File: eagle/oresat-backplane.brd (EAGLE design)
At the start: 82.8 x 213.8 mm, 98 parts

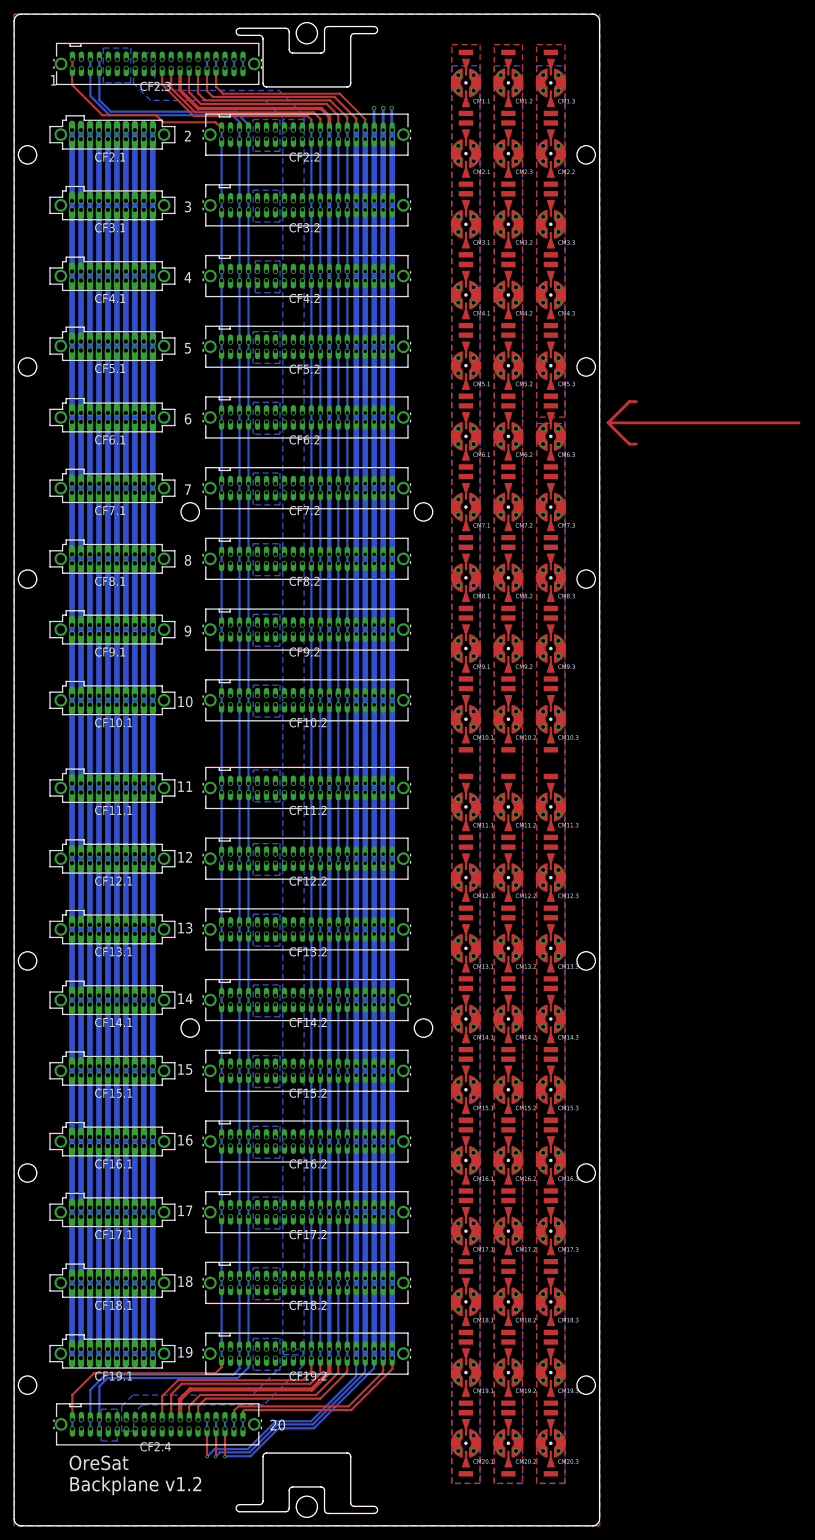
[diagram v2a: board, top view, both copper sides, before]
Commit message: Updated connector locations from MCAD. Last of the separate RF grounds before reverting back to single ground plane.
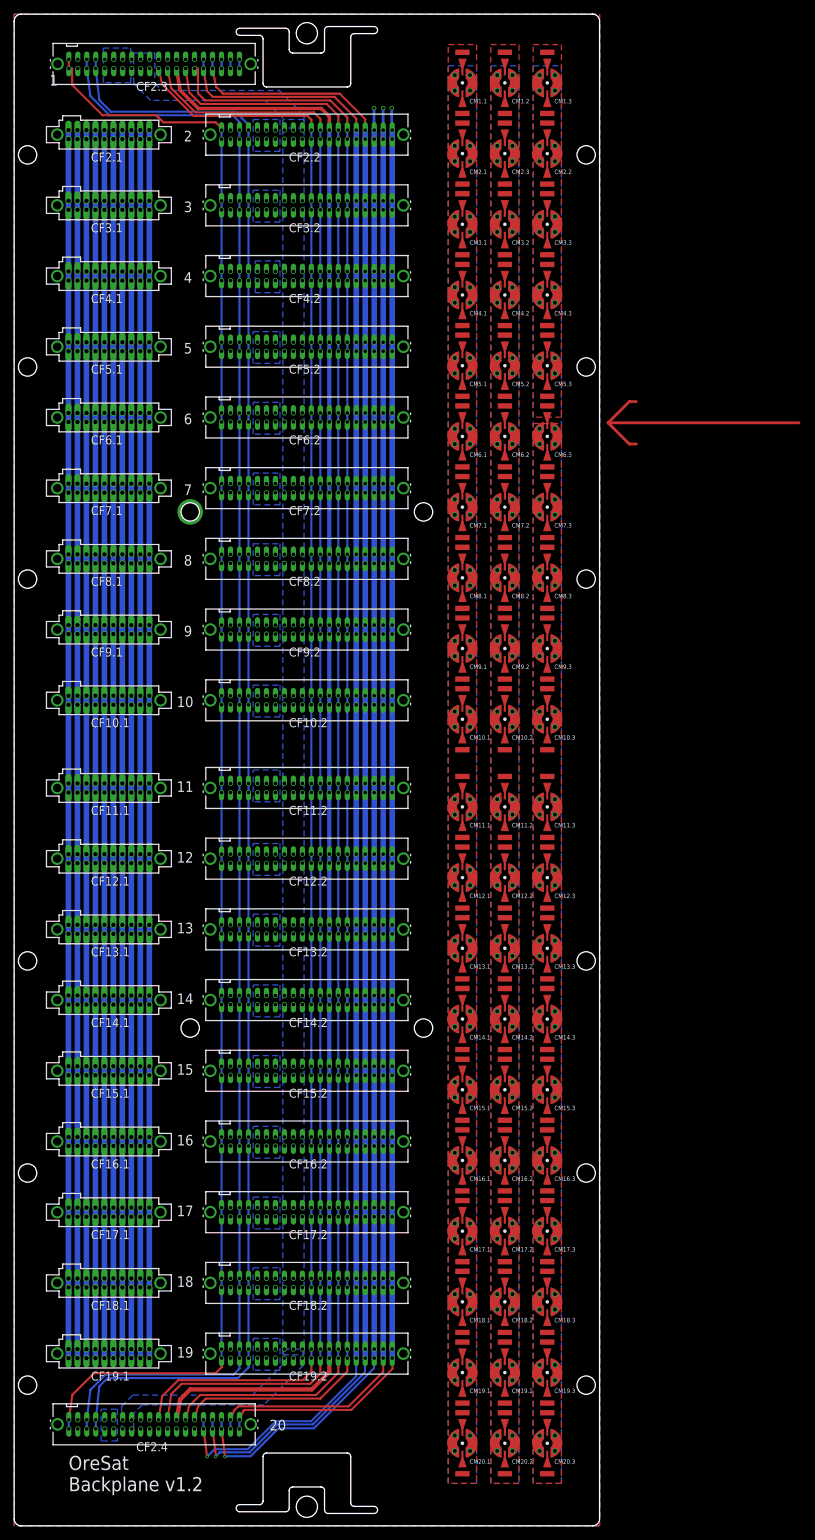
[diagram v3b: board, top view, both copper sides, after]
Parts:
- moved CF5.1 0.51 mm to (13.4, 166.8)
- moved CF10.1 0.50 mm to (13.4, 116.8)
- moved CF11.1 0.50 mm to (13.4, 104.4)
- moved CF12.1 0.50 mm to (13.4, 94.4)
- moved CF13.1 0.50 mm to (13.4, 84.4)
- moved CF14.1 0.50 mm to (13.4, 74.4)
- moved CF15.1 0.50 mm to (13.4, 64.4)
- moved CF16.1 0.50 mm to (13.4, 54.4)
- moved CF17.1 0.50 mm to (13.4, 44.4)
- moved CF18.1 0.50 mm to (13.4, 34.4)
- moved CF19.1 0.50 mm to (13.4, 24.4)
- moved CF2.1 0.50 mm to (13.4, 196.8)
- moved CF2.3 0.50 mm to (19.8, 206.8)
- moved CF2.4 0.50 mm to (19.8, 14.4)
- moved CF3.1 0.50 mm to (13.4, 186.8)
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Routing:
- net !SD: track 230.1 -> 231.0 mm
- net OPD_SDA: track 229.8 -> 230.3 mm

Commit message: Backplane v2.0! New dimensions and connector placement for Frame v1.1. New bespoke RF lines for the current OreSat RF card and antenna plan. After design review, added one more pin pair to vbus and gnd. Killed two spare pins, down to 5. Still some waffling on microsptrip width, otherwise done.
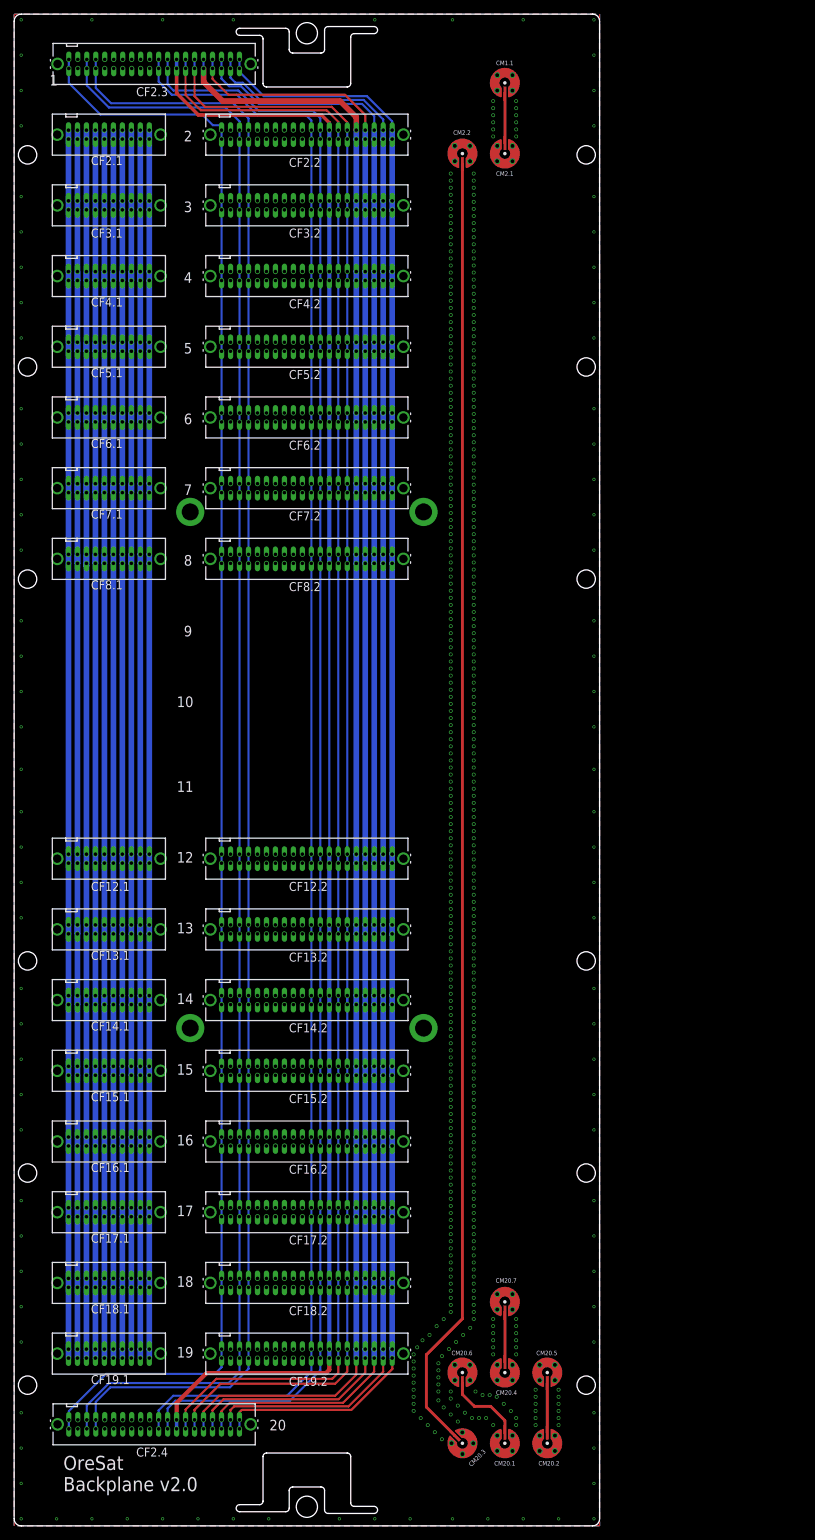
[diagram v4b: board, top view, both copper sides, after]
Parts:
- removed CF10.1, CF11.1, CF9.1: SFM-110-X1-XXX-D-LC, J-Samtec-SFM-110-X1-XXX-D-LC:SFM-110-X1-XXX-D-LC
- removed CF10.2, CF11.2, CF9.2: SFM-120-X1-XXX-D, J-Samtec-SFM-120-X1-XXX-D:SFM-120-X1-XXX-D
- removed CM1.2, CM1.3, CM10.1, CM10.2, CM10.3, CM11.1, CM11.2, CM11.3, CM12.1, CM12.2, CM12.3, CM13.1, CM13.2, CM13.3, CM14.1, CM14.2, CM14.3, CM15.1, CM15.2, CM15.3, CM16.1, CM16.2, CM16.3, CM17.1, CM17.2, CM17.3, CM18.1, CM18.2, CM18.3, CM19.1, CM19.2, CM19.3, CM2.3, CM3.1, CM3.2, CM3.3, CM4.1, CM4.2, CM4.3, CM5.1, CM5.2, CM5.3, CM6.1, CM6.2, CM6.3, CM7.1, CM7.2, CM7.3, CM8.1, CM8.2, CM8.3, CM9.1, CM9.2, CM9.3: J-MOLEX-SMPM-73300-0111X, J-Molex-SMPM-73300-011x:J-MOLEX-SMPM-73300-0111X
- added CM20.4, CM20.5, CM20.6, CM20.7: J-MOLEX-SMPM-73300-0111X, J-Molex-73300-011x-SMPM-M-vertical:J-MOLEX-SMPM-73300-0111X
- CM1.1, CM2.1, CM2.2, CM20.1, CM20.2, CM20.3: device J-Molex-SMPM-73300-011x:J-MOLEX-SMPM-73300-0111X -> J-Molex-73300-011x-SMPM-M-vertical:J-MOLEX-SMPM-73300-0111X
- moved CM2.2 12.0 mm to (63.4, 194.1), turned to 180 degrees
- moved CM20.3 12.0 mm to (63.4, 11.7), turned to 45 degrees
- moved CM1.1 6.00 mm to (69.4, 204.1), turned to 180 degrees
- moved CM2.1 6.00 mm to (69.4, 194.1)
- moved CM20.1 6.00 mm to (69.4, 11.7)
- moved CM20.2 6.00 mm to (75.4, 11.7)
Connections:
- removed net GND1: CM1.1.P$1, CM1.1.P$2, CM1.1.P$3, CM1.1.P$4, CM1.1.P$5, CM1.1.P$6, CM10.1.P$1, CM10.1.P$2, CM10.1.P$3, CM10.1.P$4, CM10.1.P$5, CM10.1.P$6, CM11.1.P$1, CM11.1.P$2, CM11.1.P$3, CM11.1.P$4, CM11.1.P$5, CM11.1.P$6, CM12.1.P$1, CM12.1.P$2, CM12.1.P$3, CM12.1.P$4, CM12.1.P$5, CM12.1.P$6, CM13.1.P$1, CM13.1.P$2, CM13.1.P$3, CM13.1.P$4, CM13.1.P$5, CM13.1.P$6, CM14.1.P$1, CM14.1.P$2, CM14.1.P$3, CM14.1.P$4, CM14.1.P$5, CM14.1.P$6, CM15.1.P$1, CM15.1.P$2, CM15.1.P$3, CM15.1.P$4, CM15.1.P$5, CM15.1.P$6, CM16.1.P$1, CM16.1.P$2, CM16.1.P$3, CM16.1.P$4, CM16.1.P$5, CM16.1.P$6, CM17.1.P$1, CM17.1.P$2, CM17.1.P$3, CM17.1.P$4, CM17.1.P$5, CM17.1.P$6, CM18.1.P$1, CM18.1.P$2, CM18.1.P$3, CM18.1.P$4, CM18.1.P$5, CM18.1.P$6, CM19.1.P$1, CM19.1.P$2, CM19.1.P$3, CM19.1.P$4, CM19.1.P$5, CM19.1.P$6, CM2.1.P$1, CM2.1.P$2, CM2.1.P$3, CM2.1.P$4, CM2.1.P$5, CM2.1.P$6, CM20.1.P$1, CM20.1.P$2, CM20.1.P$3, CM20.1.P$4, CM20.1.P$5, CM20.1.P$6, CM3.1.P$1, CM3.1.P$2, CM3.1.P$3, CM3.1.P$4, CM3.1.P$5, CM3.1.P$6, CM4.1.P$1, CM4.1.P$2, CM4.1.P$3, CM4.1.P$4, CM4.1.P$5, CM4.1.P$6, CM5.1.P$1, CM5.1.P$2, CM5.1.P$3, CM5.1.P$4, CM5.1.P$5, CM5.1.P$6, CM6.1.P$1, CM6.1.P$2, CM6.1.P$3, CM6.1.P$4, CM6.1.P$5, CM6.1.P$6, CM7.1.P$1, CM7.1.P$2, CM7.1.P$3, CM7.1.P$4, CM7.1.P$5, CM7.1.P$6, CM8.1.P$1, CM8.1.P$2, CM8.1.P$3, CM8.1.P$4, CM8.1.P$5, CM8.1.P$6, CM9.1.P$1, CM9.1.P$2, CM9.1.P$3, CM9.1.P$4, CM9.1.P$5, CM9.1.P$6
- removed net GND2: CM1.2.P$1, CM1.2.P$2, CM1.2.P$3, CM1.2.P$4, CM1.2.P$5, CM1.2.P$6, CM10.2.P$1, CM10.2.P$2, CM10.2.P$3, CM10.2.P$4, CM10.2.P$5, CM10.2.P$6, CM11.2.P$1, CM11.2.P$2, CM11.2.P$3, CM11.2.P$4, CM11.2.P$5, CM11.2.P$6, CM12.2.P$1, CM12.2.P$2, CM12.2.P$3, CM12.2.P$4, CM12.2.P$5, CM12.2.P$6, CM13.2.P$1, CM13.2.P$2, CM13.2.P$3, CM13.2.P$4, CM13.2.P$5, CM13.2.P$6, CM14.2.P$1, CM14.2.P$2, CM14.2.P$3, CM14.2.P$4, CM14.2.P$5, CM14.2.P$6, CM15.2.P$1, CM15.2.P$2, CM15.2.P$3, CM15.2.P$4, CM15.2.P$5, CM15.2.P$6, CM16.2.P$1, CM16.2.P$2, CM16.2.P$3, CM16.2.P$4, CM16.2.P$5, CM16.2.P$6, CM17.2.P$1, CM17.2.P$2, CM17.2.P$3, CM17.2.P$4, CM17.2.P$5, CM17.2.P$6, CM18.2.P$1, CM18.2.P$2, CM18.2.P$3, CM18.2.P$4, CM18.2.P$5, CM18.2.P$6, CM19.2.P$1, CM19.2.P$2, CM19.2.P$3, CM19.2.P$4, CM19.2.P$5, CM19.2.P$6, CM2.3.P$1, CM2.3.P$2, CM2.3.P$3, CM2.3.P$4, CM2.3.P$5, CM2.3.P$6, CM20.2.P$1, CM20.2.P$2, CM20.2.P$3, CM20.2.P$4, CM20.2.P$5, CM20.2.P$6, CM3.2.P$1, CM3.2.P$2, CM3.2.P$3, CM3.2.P$4, CM3.2.P$5, CM3.2.P$6, CM4.2.P$1, CM4.2.P$2, CM4.2.P$3, CM4.2.P$4, CM4.2.P$5, CM4.2.P$6, CM5.2.P$1, CM5.2.P$2, CM5.2.P$3, CM5.2.P$4, CM5.2.P$5, CM5.2.P$6, CM6.2.P$1, CM6.2.P$2, CM6.2.P$3, CM6.2.P$4, CM6.2.P$5, CM6.2.P$6, CM7.2.P$1, CM7.2.P$2, CM7.2.P$3, CM7.2.P$4, CM7.2.P$5, CM7.2.P$6, CM8.2.P$1, CM8.2.P$2, CM8.2.P$3, CM8.2.P$4, CM8.2.P$5, CM8.2.P$6, CM9.2.P$1, CM9.2.P$2, CM9.2.P$3, CM9.2.P$4, CM9.2.P$5, CM9.2.P$6
- removed net GND3: CM1.3.P$1, CM1.3.P$2, CM1.3.P$3, CM1.3.P$4, CM1.3.P$5, CM1.3.P$6, CM10.3.P$1, CM10.3.P$2, CM10.3.P$3, CM10.3.P$4, CM10.3.P$5, CM10.3.P$6, CM11.3.P$1, CM11.3.P$2, CM11.3.P$3, CM11.3.P$4, CM11.3.P$5, CM11.3.P$6, CM12.3.P$1, CM12.3.P$2, CM12.3.P$3, CM12.3.P$4, CM12.3.P$5, CM12.3.P$6, CM13.3.P$1, CM13.3.P$2, CM13.3.P$3, CM13.3.P$4, CM13.3.P$5, CM13.3.P$6, CM14.3.P$1, CM14.3.P$2, CM14.3.P$3, CM14.3.P$4, CM14.3.P$5, CM14.3.P$6, CM15.3.P$1, CM15.3.P$2, CM15.3.P$3, CM15.3.P$4, CM15.3.P$5, CM15.3.P$6, CM16.3.P$1, CM16.3.P$2, CM16.3.P$3, CM16.3.P$4, CM16.3.P$5, CM16.3.P$6, CM17.3.P$1, CM17.3.P$2, CM17.3.P$3, CM17.3.P$4, CM17.3.P$5, CM17.3.P$6, CM18.3.P$1, CM18.3.P$2, CM18.3.P$3, CM18.3.P$4, CM18.3.P$5, CM18.3.P$6, CM19.3.P$1, CM19.3.P$2, CM19.3.P$3, CM19.3.P$4, CM19.3.P$5, CM19.3.P$6, CM2.2.P$1, CM2.2.P$2, CM2.2.P$3, CM2.2.P$4, CM2.2.P$5, CM2.2.P$6, CM20.3.P$1, CM20.3.P$2, CM20.3.P$3, CM20.3.P$4, CM20.3.P$5, CM20.3.P$6, CM3.3.P$1, CM3.3.P$2, CM3.3.P$3, CM3.3.P$4, CM3.3.P$5, CM3.3.P$6, CM4.3.P$1, CM4.3.P$2, CM4.3.P$3, CM4.3.P$4, CM4.3.P$5, CM4.3.P$6, CM5.3.P$1, CM5.3.P$2, CM5.3.P$3, CM5.3.P$4, CM5.3.P$5, CM5.3.P$6, CM6.3.P$1, CM6.3.P$2, CM6.3.P$3, CM6.3.P$4, CM6.3.P$5, CM6.3.P$6, CM7.3.P$1, CM7.3.P$2, CM7.3.P$3, CM7.3.P$4, CM7.3.P$5, CM7.3.P$6, CM8.3.P$1, CM8.3.P$2, CM8.3.P$3, CM8.3.P$4, CM8.3.P$5, CM8.3.P$6, CM9.3.P$1, CM9.3.P$2, CM9.3.P$3, CM9.3.P$4, CM9.3.P$5, CM9.3.P$6
- new net L-GPS: CM20.4.RF-DOWN, CM20.7.RF-DOWN
- new net L-TURNSTILE: CM20.2.RF-DOWN, CM20.5.RF-DOWN
- new net S-HELICAL: CM1.1.RF-DOWN, CM2.1.RF-DOWN
- new net S-TURNSTILE: CM2.2.RF-DOWN, CM20.3.RF-DOWN
- new net VHF-TURNSTILE: CM20.1.RF-DOWN, CM20.6.RF-DOWN
- net !SD: no longer CF10.2.39, CF10.2.40, CF11.2.39, CF11.2.40, CF9.2.39, CF9.2.40
- net AUX-1: no longer CF10.1.1, CF10.1.2, CF11.1.1, CF11.1.2, CF9.1.1, CF9.1.2
- net AUX-10: no longer CF10.1.19, CF10.1.20, CF11.1.19, CF11.1.20, CF9.1.19, CF9.1.20
- net AUX-2: no longer CF10.1.3, CF10.1.4, CF11.1.3, CF11.1.4, CF9.1.3, CF9.1.4
- net AUX-3: no longer CF10.1.5, CF10.1.6, CF11.1.5, CF11.1.6, CF9.1.5, CF9.1.6
- net AUX-4: no longer CF10.1.7, CF10.1.8, CF11.1.7, CF11.1.8, CF9.1.7, CF9.1.8
- net AUX-5: no longer CF10.1.10, CF10.1.9, CF11.1.10, CF11.1.9, CF9.1.10, CF9.1.9
- net AUX-6: no longer CF10.1.11, CF10.1.12, CF11.1.11, CF11.1.12, CF9.1.11, CF9.1.12
- net AUX-7: no longer CF10.1.13, CF10.1.14, CF11.1.13, CF11.1.14, CF9.1.13, CF9.1.14
- net AUX-8: no longer CF10.1.15, CF10.1.16, CF11.1.15, CF11.1.16, CF9.1.15, CF9.1.16
- net AUX-9: no longer CF10.1.17, CF10.1.18, CF11.1.17, CF11.1.18, CF9.1.17, CF9.1.18
- net CAN1_H: no longer CF10.2.33, CF10.2.34, CF11.2.33, CF11.2.34, CF9.2.33, CF9.2.34
- net CAN1_L: no longer CF10.2.35, CF10.2.36, CF11.2.35, CF11.2.36, CF9.2.35, CF9.2.36
- net CAN2_H: no longer CF10.2.17, CF10.2.18, CF11.2.17, CF11.2.18, CF9.2.17, CF9.2.18
- net CAN2_L: no longer CF10.2.19, CF10.2.20, CF11.2.19, CF11.2.20, CF9.2.19, CF9.2.20
- net GND: now also CM1.1.P$1, CM1.1.P$2, CM1.1.P$3, CM1.1.P$4, CM2.1.P$1, CM2.1.P$2, CM2.1.P$3, CM2.1.P$4, CM2.2.P$1, CM2.2.P$2, CM2.2.P$3, CM2.2.P$4, CM20.1.P$1, CM20.1.P$2, CM20.1.P$3, CM20.1.P$4, CM20.2.P$1, CM20.2.P$2, CM20.2.P$3, CM20.2.P$4, CM20.3.P$1, CM20.3.P$2, CM20.3.P$3, CM20.3.P$4, CM20.4.P$1, CM20.4.P$2, CM20.4.P$3, CM20.4.P$4, CM20.5.P$1, CM20.5.P$2, CM20.5.P$3, CM20.5.P$4, CM20.6.P$1, CM20.6.P$2, CM20.6.P$3, CM20.6.P$4, CM20.7.P$1, CM20.7.P$2, CM20.7.P$3, CM20.7.P$4; no longer CF10.1.LC1, CF10.1.LC2, CF10.2.27, CF10.2.28, CF10.2.29, CF10.2.30, CF10.2.31, CF10.2.32, CF10.2.37, CF10.2.38, CF10.2.LC1, CF10.2.LC2, CF11.1.LC1, CF11.1.LC2, CF11.2.27, CF11.2.28, CF11.2.29, CF11.2.30, CF11.2.31, CF11.2.32, CF11.2.37, CF11.2.38, CF11.2.LC1, CF11.2.LC2, CF9.1.LC1, CF9.1.LC2, CF9.2.27, CF9.2.28, CF9.2.29, CF9.2.30, CF9.2.31, CF9.2.32, CF9.2.37, CF9.2.38, CF9.2.LC1, CF9.2.LC2
- net OPD_PWR: no longer CF10.2.15, CF10.2.16, CF11.2.15, CF11.2.16, CF9.2.15, CF9.2.16
- net OPD_SCL: no longer CF10.2.13, CF10.2.14, CF11.2.13, CF11.2.14, CF9.2.13, CF9.2.14
- net OPD_SDA: no longer CF10.2.11, CF10.2.12, CF11.2.11, CF11.2.12, CF9.2.11, CF9.2.12
- net SPARE1: no longer CF10.2.10, CF10.2.9, CF11.2.10, CF11.2.9, CF9.2.10, CF9.2.9
- net SPARE2: no longer CF10.2.7, CF10.2.8, CF11.2.7, CF11.2.8, CF9.2.7, CF9.2.8
- net SPARE3: no longer CF10.2.5, CF10.2.6, CF11.2.5, CF11.2.6, CF9.2.5, CF9.2.6
- net SPARE4: no longer CF10.2.3, CF10.2.4, CF11.2.3, CF11.2.4, CF9.2.3, CF9.2.4
- net SPARE5: no longer CF10.2.1, CF10.2.2, CF11.2.1, CF11.2.2, CF9.2.1, CF9.2.2
- net VBUS: no longer CF10.2.21, CF10.2.22, CF10.2.23, CF10.2.24, CF10.2.25, CF10.2.26, CF11.2.21, CF11.2.22, CF11.2.23, CF11.2.24, CF11.2.25, CF11.2.26, CF9.2.21, CF9.2.22, CF9.2.23, CF9.2.24, CF9.2.25, CF9.2.26
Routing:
- net S-TURNSTILE: track 0.00 -> 183.6 mm
- net N$1: track 37.5 -> 0.00 mm
- net SPARE4: track 206.0 -> 230.3 mm, vias 1 -> 0
- net SPARE5: track 205.8 -> 229.2 mm, vias 1 -> 0
- net SPARE3: track 211.0 -> 230.5 mm, vias 2 -> 0
- net VHF-TURNSTILE: track 0.00 -> 10.8 mm
- net S-HELICAL: track 0.00 -> 7.00 mm
- net L-TURNSTILE: track 0.00 -> 7.00 mm
- net L-GPS: track 0.00 -> 7.00 mm
- net SPARE1: track 236.1 -> 230.9 mm, vias 1 -> 0
- net AUX-9: track 187.6 -> 182.6 mm
- net AUX-7: track 185.1 -> 180.0 mm
- net AUX-6: track 186.4 -> 181.3 mm
- net AUX-5: track 183.8 -> 178.8 mm
- net AUX-4: track 182.6 -> 177.5 mm
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- added copper zone on layer 15, net GND
- added copper zone on layer 2, net GND
- added copper zone on layer 15, net VBUS
- removed copper zone on layer 1, net GND1
- removed copper zone on layer 16, net GND1
- removed copper zone on layer 1, net GND2
- removed copper zone on layer 16, net GND2
- removed copper zone on layer 1, net GND3
- removed copper zone on layer 16, net GND3
- removed copper zone on layer 16, net VBUS
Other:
- board text added: "Backplane v2.0"
- board text added: "OreSat Backplane v2.0"
- board text removed: "Backplane v1.2"
- board text removed: "OreSat Backplane v1.2"

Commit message: Updated microstrips to 0.38 mm based on theoretical calcs of 0.35 mm for the OSH Park 4 layer, and Harmon Industry's measurements of 0.41 mm for 50 ohms. Also expanded solder mask openings around RF lines, fixed weirdly thick traces on the backplanes.
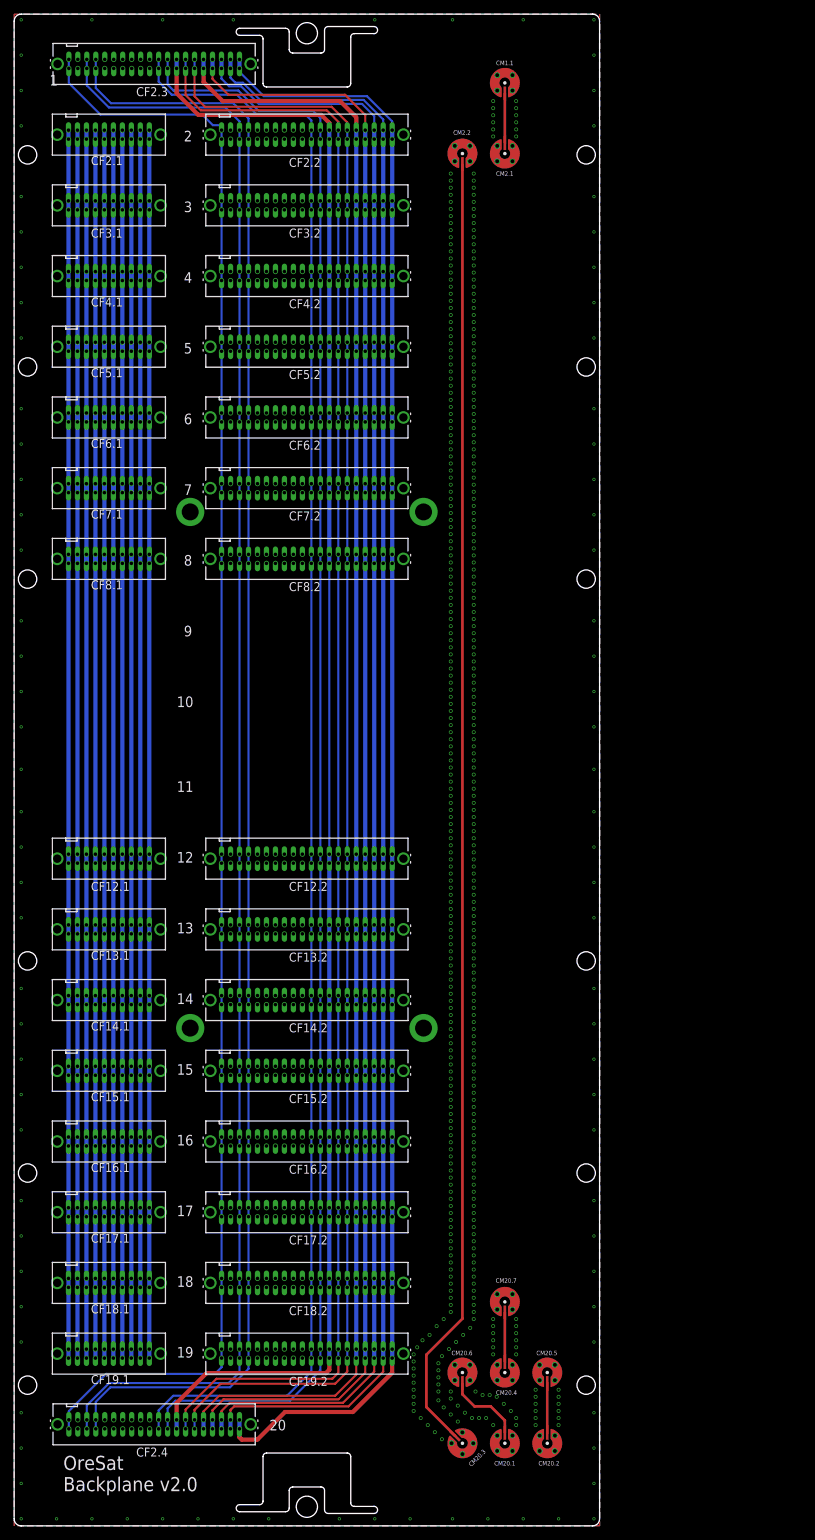
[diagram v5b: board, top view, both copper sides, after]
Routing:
- net SPARE5: track 229.2 -> 231.3 mm
